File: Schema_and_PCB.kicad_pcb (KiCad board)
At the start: 2 copper layers, 0 parts

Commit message: board setup is done
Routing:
- net (no net): vias 0 -> 1
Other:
- copper layers 2 -> 4
- net class Default: trace_width 0.25 -> 0.2; via_dia 0.8 -> 0.6; via_drill 0.4 -> 0.3
- net class Power added: clearance 0.2, trace_width 0.6, via_dia 0.6, via_drill 0.3
- net class Thin added: clearance 0.2, trace_width 0.15, via_dia 0.6, via_drill 0.3
- rule trace_min: 0.15 -> 0.125
- rule via_min_size: 0.4 -> 0.3
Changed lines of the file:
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@@
 (kicad_pcb (version 20171130) (host pcbnew 5.1.10-88a1d61d58~88~ubuntu20.04.1)
   (general
-    (thickness 1.6)
+    (thickness 2)
     (drawings 0)
-    (tracks 0)
+    (tracks 1)
     (zones 0)
     (modules 0)
     (nets 1)
   )
-  (page A4)
+  (page A3)
   (title_block
-    (date 2021-03-19)
+    (title ШВУ)
+    (date 2021-05-21)
+    (rev v0.1)
+    (company SVIELCOM)
   )
   (layers
-    (0 F.Cu signal)
-    (31 B.Cu signal)
+    (0 F.Cu mixed)
+    (1 In1.Cu jumper)
+    (2 In2.Cu mixed)
+    (31 B.Cu mixed)
     (32 B.Adhes user)
     (33 F.Adhes user)
@@
   )
   (setup
-    (last_trace_width 0.25)
+    (last_trace_width 0.2)
     (user_trace_width 0.15)
+    (user_trace_width 0.2)
+    (user_trace_width 0.6)
     (trace_clearance 0.2)
     (zone_clearance 0.508)
     (zone_45_only no)
-    (trace_min 0.15)
-    (via_size 0.8)
-    (via_drill 0.4)
-    (via_min_size 0.4)
+    (trace_min 0.125)
+    (via_size 0.6)
+    (via_drill 0.3)
+    (via_min_size 0.3)
     (via_min_drill 0.3)
+    (user_via 0.6 0.3)
+    (user_via 0.8 0.5)
     (uvia_size 0.3)
     (uvia_drill 0.1)
@@
     (uvia_min_drill 0.1)
     (edge_width 0.1)
-    (segment_width 0.2)
+    (segment_width 0.25)
     (pcb_text_width 0.3)
     (pcb_text_size 1.5 1.5)
@@
   (net_class Default "This is the default net class."
     (clearance 0.2)
-    (trace_width 0.25)
-    (via_dia 0.8)
-    (via_drill 0.4)
+    (trace_width 0.2)
+    (via_dia 0.6)
+    (via_drill 0.3)
     (uvia_dia 0.3)
     (uvia_drill 0.1)
   )
+  (net_class Power ""
+    (clearance 0.2)
+    (trace_width 0.6)
+    (via_dia 0.6)
+    (via_drill 0.3)
+    (uvia_dia 0.3)
+    (uvia_drill 0.1)
+  )
+  (net_class Thin ""
+    (clearance 0.2)
+    (trace_width 0.15)
+    (via_dia 0.6)
+    (via_drill 0.3)
+    (uvia_dia 0.3)
+    (uvia_drill 0.1)
+  )
+  (via (at 169.4688 109.0676) (size 0.6) (drill 0.3) (layers F.Cu B.Cu) (net 0))
 )

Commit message: board shape is done
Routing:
- net (no net): vias 1 -> 0
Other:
- board outline added: 294.6 x 143.3 mm
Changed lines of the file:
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@@
   (general
     (thickness 2)
-    (drawings 0)
-    (tracks 1)
+    (drawings 41)
+    (tracks 0)
     (zones 0)
     (modules 0)
@@
     (uvia_drill 0.1)
   )
-  (via (at 169.4688 109.0676) (size 0.6) (drill 0.3) (layers F.Cu B.Cu) (net 0))
+  (gr_circle (center 347.726 92.9259) (end 349.7326 92.9259) (layer Edge.Cuts) (width 0.1))
+  (gr_circle (center 347.726 187.9346) (end 349.7326 187.9346) (layer Edge.Cuts) (width 0.1))
+  (gr_circle (center 215.6079 161.4551) (end 217.6145 161.4551) (layer Edge.Cuts) (width 0.1))
+  (gr_circle (center 68.6562 191.0969) (end 70.6628 191.0969) (layer Edge.Cuts) (width 0.1))
+  (gr_circle (center 68.6562 96.1009) (end 70.6628 96.1009) (layer Edge.Cuts) (width 0.1))
+  (gr_arc (start 63.0682 200.0123) (end 61.6458 200.0123) (angle -90) (layer Edge.Cuts) (width 0.1))
+  (gr_arc (start 81.2165 202.8571) (end 82.6389 202.8571) (angle -90) (layer Edge.Cuts) (width 0.1))
+  (gr_arc (start 84.0613 213.0171) (end 82.6389 213.0171) (angle -90) (layer Edge.Cuts) (width 0.1))
+  (gr_arc (start 193.8147 213.0171) (end 193.8147 214.4395) (angle -90) (layer Edge.Cuts) (width 0.1))
+  (gr_arc (start 196.6595 182.0926) (end 196.6595 180.6702) (angle -90) (layer Edge.Cuts) (width 0.1))
+  (gr_arc (start 337.82 182.0926) (end 339.2424 182.0926) (angle -90) (layer Edge.Cuts) (width 0.1))
+  (gr_arc (start 340.6648 194.9323) (end 339.2424 194.9323) (angle -90) (layer Edge.Cuts) (width 0.1))
+  (gr_arc (start 354.8126 194.9323) (end 354.8126 196.3547) (angle -90) (layer Edge.Cuts) (width 0.1))
+  (gr_arc (start 354.8126 86.8172) (end 356.235 86.8172) (angle -90) (layer Edge.Cuts) (width 0.1))
+  (gr_arc (start 333.6544 83.9724) (end 332.232 83.9724) (angle -90) (layer Edge.Cuts) (width 0.1))
+  (gr_arc (start 330.8096 72.5297) (end 332.232 72.5297) (angle -90) (layer Edge.Cuts) (width 0.1))
+  (gr_arc (start 220.6498 72.5297) (end 220.6498 71.1073) (angle -90) (layer Edge.Cuts) (width 0.1))
+  (gr_arc (start 217.805 78.6511) (end 217.805 80.0735) (angle -90) (layer Edge.Cuts) (width 0.1))
+  (gr_arc (start 192.7987 72.5297) (end 194.2211 72.5297) (angle -90) (layer Edge.Cuts) (width 0.1))
+  (gr_arc (start 195.6435 78.6511) (end 194.2211 78.6511) (angle -90) (layer Edge.Cuts) (width 0.1))
+  (gr_arc (start 84.074 72.5297) (end 84.074 71.1073) (angle -90) (layer Edge.Cuts) (width 0.1))
+  (gr_arc (start 63.0682 87.4649) (end 63.0682 86.0425) (angle -90) (layer Edge.Cuts) (width 0.1))
+  (gr_arc (start 81.2292 84.6201) (end 81.2292 86.0425) (angle -90) (layer Edge.Cuts) (width 0.1))
+  (gr_line (start 356.235 86.8172) (end 356.235 194.9323) (layer Edge.Cuts) (width 0.1))
+  (gr_line (start 333.6544 85.3948) (end 354.8126 85.3948) (layer Edge.Cuts) (width 0.1))
+  (gr_line (start 332.232 72.5297) (end 332.232 83.9724) (layer Edge.Cuts) (width 0.1))
+  (gr_line (start 220.6498 71.1073) (end 330.8096 71.1073) (layer Edge.Cuts) (width 0.1))
+  (gr_line (start 219.2274 78.6511) (end 219.2274 72.5297) (layer Edge.Cuts) (width 0.1))
+  (gr_line (start 195.6435 80.0735) (end 217.805 80.0735) (layer Edge.Cuts) (width 0.1))
+  (gr_line (start 194.2211 72.5297) (end 194.2211 78.6511) (layer Edge.Cuts) (width 0.1))
+  (gr_line (start 84.074 71.1073) (end 192.7987 71.1073) (layer Edge.Cuts) (width 0.1))
+  (gr_line (start 82.6516 84.6201) (end 82.6516 72.5297) (layer Edge.Cuts) (width 0.1))
+  (gr_line (start 63.0682 86.0425) (end 81.2292 86.0425) (layer Edge.Cuts) (width 0.1))
+  (gr_line (start 61.6458 200.0123) (end 61.6458 87.4649) (layer Edge.Cuts) (width 0.1))
+  (gr_line (start 81.2165 201.4347) (end 63.0682 201.4347) (layer Edge.Cuts) (width 0.1))
+  (gr_line (start 82.6389 213.0171) (end 82.6389 202.8571) (layer Edge.Cuts) (width 0.1))
+  (gr_line (start 193.8147 214.4395) (end 84.0613 214.4395) (layer Edge.Cuts) (width 0.1))
+  (gr_line (start 195.2371 182.0926) (end 195.2371 213.0171) (layer Edge.Cuts) (width 0.1))
+  (gr_line (start 337.82 180.6702) (end 196.6595 180.6702) (layer Edge.Cuts) (width 0.1))
+  (gr_line (start 339.2424 194.9323) (end 339.2424 182.0926) (layer Edge.Cuts) (width 0.1))
+  (gr_line (start 354.8126 196.3547) (end 340.6648 196.3547) (layer Edge.Cuts) (width 0.1))
 )

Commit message: starting PCB layout
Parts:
- added BT1: CR2032, SVIELCOM:BAT_BS-7, F.Cu at (13.6, 21.3)
- added C1: 10µF, Capacitor_Tantalum_SMD:CP_EIA-3216-10_Kemet-I, F.Cu at (250.7, 253.4)
- added C10: 2,7pF, Capacitor_SMD:C_0603_1608Metric_Pad1.08x0.95mm_HandSolder, F.Cu at (24.8, 40.1)
- added C11: 47µFx16, Capacitor_Tantalum_SMD:CP_EIA-7343-31_Kemet-D_Pad2.25x2.55mm_HandSolder, F.Cu at (16.2, 45.8)
- added C12: 10µFx16, Capacitor_Tantalum_SMD:CP_EIA-3216-10_Kemet-I, F.Cu at (34.5, 47.6)
- added C13: 1µF, Capacitor_SMD:C_0603_1608Metric_Pad1.08x0.95mm_HandSolder, F.Cu at (66.5, 23.7)
- added C14: 0,1µF, Capacitor_SMD:C_0603_1608Metric_Pad1.08x0.95mm_HandSolder, F.Cu at (68.6, 26.2)
- added C15: 47µFx16, Capacitor_Tantalum_SMD:CP_EIA-7343-31_Kemet-D_Pad2.25x2.55mm_HandSolder, F.Cu at (26.5, 45.8)
- added C16: 10µFx16, Capacitor_Tantalum_SMD:CP_EIA-3216-10_Kemet-I, F.Cu at (43.4, 43.0)
- added C17: 1µF, Capacitor_SMD:C_0603_1608Metric_Pad1.08x0.95mm_HandSolder, F.Cu at (61.4, 37.8)
- added C18: 1µF, Capacitor_SMD:C_0603_1608Metric_Pad1.08x0.95mm_HandSolder, F.Cu at (57.1, 40.3)
- added C19: 1µF, Capacitor_SMD:C_0603_1608Metric_Pad1.08x0.95mm_HandSolder, F.Cu at (68.6, 28.7)
- added C2: 1µF, Capacitor_SMD:C_0603_1608Metric_Pad1.08x0.95mm_HandSolder, F.Cu at (246.0, 253.2)
- added C20: 1µF, Capacitor_SMD:C_0603_1608Metric_Pad1.08x0.95mm_HandSolder, F.Cu at (61.6, 35.3)
- added C21: 1µF, Capacitor_SMD:C_0603_1608Metric_Pad1.08x0.95mm_HandSolder, F.Cu at (71.3, 20.8)
- added C22: 1µF, Capacitor_SMD:C_0603_1608Metric_Pad1.08x0.95mm_HandSolder, F.Cu at (48.2, 47.7)
- added C23: 1µF, Capacitor_SMD:C_0603_1608Metric_Pad1.08x0.95mm_HandSolder, F.Cu at (61.6, 32.8)
- added C24: 1µF, Capacitor_SMD:C_0603_1608Metric_Pad1.08x0.95mm_HandSolder, F.Cu at (43.8, 48.4)
- added C25: 1µF, Capacitor_SMD:C_0603_1608Metric_Pad1.08x0.95mm_HandSolder, F.Cu at (42.7, 50.9)
- added C26: 1µF, Capacitor_SMD:C_0603_1608Metric_Pad1.08x0.95mm_HandSolder, F.Cu at (70.9, 23.3)
- added C27: 1µF, Capacitor_SMD:C_0603_1608Metric_Pad1.08x0.95mm_HandSolder, F.Cu at (57.1, 37.8)
- added C28: 10µF, Capacitor_Tantalum_SMD:CP_EIA-3216-10_Kemet-I, F.Cu at (34.5, 44.5)
- added C29: 2,2µF, Capacitor_SMD:C_0603_1608Metric_Pad1.08x0.95mm_HandSolder, F.Cu at (57.3, 35.3)
- added C3: 1µF, Capacitor_SMD:C_0603_1608Metric_Pad1.08x0.95mm_HandSolder, F.Cu at (291.1, 248.5)
- added C30: 2,2µF, Capacitor_SMD:C_0603_1608Metric_Pad1.08x0.95mm_HandSolder, F.Cu at (64.3, 28.7)
- added C31: 1µF, Capacitor_SMD:C_0603_1608Metric_Pad1.08x0.95mm_HandSolder, F.Cu at (48.4, 45.2)
- added C32: 10µF, Capacitor_Tantalum_SMD:CP_EIA-3216-10_Kemet-I, F.Cu at (23.0, 50.3)
- added C33: 1µF, Capacitor_SMD:C_0603_1608Metric_Pad1.08x0.95mm_HandSolder, F.Cu at (52.7, 43.5)
- added C34: 10µF, Capacitor_Tantalum_SMD:CP_EIA-3216-10_Kemet-I, F.Cu at (61.6, 19.4)
- added C35: 1µF, Capacitor_SMD:C_0603_1608Metric_Pad1.08x0.95mm_HandSolder, F.Cu at (64.3, 26.2)
- added C36: 1µF, Capacitor_SMD:C_0603_1608Metric_Pad1.08x0.95mm_HandSolder, F.Cu at (57.3, 32.8)
- added C37: 1µF, Capacitor_SMD:C_0603_1608Metric_Pad1.08x0.95mm_HandSolder, F.Cu at (52.5, 37.4)
- added C38: 1µF, Capacitor_SMD:C_0603_1608Metric_Pad1.08x0.95mm_HandSolder, F.Cu at (59.5, 30.3)
- added C39: 1µF, Capacitor_SMD:C_0603_1608Metric_Pad1.08x0.95mm_HandSolder, F.Cu at (71.3, 18.2)
- added C4: 1µF, Capacitor_SMD:C_0603_1608Metric_Pad1.08x0.95mm_HandSolder, F.Cu at (306.1, 240.5)
- added C40: 1µF, Capacitor_SMD:C_0603_1608Metric_Pad1.08x0.95mm_HandSolder, F.Cu at (43.8, 45.9)
- added C41: 1µF, Capacitor_SMD:C_0603_1608Metric_Pad1.08x0.95mm_HandSolder, F.Cu at (38.4, 50.9)
- added C42: 1µF, Capacitor_SMD:C_0603_1608Metric_Pad1.08x0.95mm_HandSolder, F.Cu at (39.5, 48.4)
- added C43: 1µF, Capacitor_SMD:C_0603_1608Metric_Pad1.08x0.95mm_HandSolder, F.Cu at (39.5, 45.9)
- added C44: 1µF, Capacitor_SMD:C_0603_1608Metric_Pad1.08x0.95mm_HandSolder, F.Cu at (24.8, 37.6)
- added C45: 1µF, Capacitor_SMD:C_0603_1608Metric_Pad1.08x0.95mm_HandSolder, F.Cu at (97.9, 57.7)
- added C46: 1µF, Capacitor_SMD:C_0603_1608Metric_Pad1.08x0.95mm_HandSolder, F.Cu at (211.2, 252.7)
- added C47: 1µF, Capacitor_SMD:C_0603_1608Metric_Pad1.08x0.95mm_HandSolder, F.Cu at (220.0, 252.9)
- added C48: 1µF, Capacitor_SMD:C_0603_1608Metric_Pad1.08x0.95mm_HandSolder, F.Cu at (16.2, -10.9)
- added C49: 10µFx35, Capacitor_Tantalum_SMD:CP_EIA-7343-30_AVX-N_Pad2.25x2.55mm_HandSolder, F.Cu at (31.4, -2.06)
- added C5: 4,6pF, Capacitor_SMD:C_0603_1608Metric_Pad1.08x0.95mm_HandSolder, F.Cu at (24.8, 35.0)
- added C50: 1µF, Capacitor_SMD:C_0603_1608Metric_Pad1.08x0.95mm_HandSolder, F.Cu at (38.2, -13.5)
- added C51: 10µFx35, Capacitor_Tantalum_SMD:CP_EIA-7343-30_AVX-N_Pad2.25x2.55mm_HandSolder, F.Cu at (16.5, 1.91)
- added C52: 1µF, Capacitor_SMD:C_0603_1608Metric_Pad1.08x0.95mm_HandSolder, F.Cu at (33.9, -13.5)
- added C53: 10µFx16, Capacitor_Tantalum_SMD:CP_EIA-3216-10_Kemet-I, F.Cu at (52.4, -35.6)
- added C54: 0,1µF, Capacitor_SMD:C_0603_1608Metric_Pad1.08x0.95mm_HandSolder, F.Cu at (29.5, -13.5)
- added C55: 0,1µF, Capacitor_SMD:C_0603_1608Metric_Pad1.08x0.95mm_HandSolder, F.Cu at (9.17, 4.04)
- added C56: 0,22µF, Capacitor_SMD:C_0603_1608Metric_Pad1.08x0.95mm_HandSolder, F.Cu at (59.5, 1.89)
- added C57: 330pF, Capacitor_SMD:C_0603_1608Metric_Pad1.08x0.95mm_HandSolder, F.Cu at (72.3, -9.30)
- added C58: 1µF, Capacitor_SMD:C_0603_1608Metric_Pad1.08x0.95mm_HandSolder, F.Cu at (89.9, -28.4)
- added C59: 1µF, Capacitor_SMD:C_0603_1608Metric_Pad1.08x0.95mm_HandSolder, F.Cu at (80.9, -18.1)
- added C6: 4,6pF, Capacitor_SMD:C_0603_1608Metric_Pad1.08x0.95mm_HandSolder, F.Cu at (48.4, 42.7)
- added C60: 10µFx35, Capacitor_Tantalum_SMD:CP_EIA-7343-30_AVX-N_Pad2.25x2.55mm_HandSolder, F.Cu at (69.6, -50.5)
- added C61: 1µF, Capacitor_SMD:C_0603_1608Metric_Pad1.08x0.95mm_HandSolder, F.Cu at (98.3, -36.6)
- added C62: 1µF, Capacitor_SMD:C_0603_1608Metric_Pad1.08x0.95mm_HandSolder, F.Cu at (76.2, -14.7)
- added C63: 0,1µF, Capacitor_SMD:C_0603_1608Metric_Pad1.08x0.95mm_HandSolder, F.Cu at (96.8, -33.9)
- added C64: 0,22µF, Capacitor_SMD:C_0603_1608Metric_Pad1.08x0.95mm_HandSolder, F.Cu at (85.7, -24.0)
- added C65: 330pF, Capacitor_SMD:C_0603_1608Metric_Pad1.08x0.95mm_HandSolder, F.Cu at (59.4, -3.13)
- added C66: 0,1µF, Capacitor_SMD:C_0603_1608Metric_Pad1.08x0.95mm_HandSolder, F.Cu at (63.8, -0.62)
- added C67: 1µF, Capacitor_SMD:C_0603_1608Metric_Pad1.08x0.95mm_HandSolder, F.Cu at (89.9, -30.9)
- added C68: 1µF, Capacitor_SMD:C_0603_1608Metric_Pad1.08x0.95mm_HandSolder, F.Cu at (59.5, -0.62)
- added C69: 1µF, Capacitor_SMD:C_0603_1608Metric_Pad1.08x0.95mm_HandSolder, F.Cu at (67.5, -6.35)
- added C7: 2,7pF, Capacitor_SMD:C_0603_1608Metric_Pad1.08x0.95mm_HandSolder, F.Cu at (66.5, 21.2)
- added C70: 1µF, Capacitor_SMD:C_0603_1608Metric_Pad1.08x0.95mm_HandSolder, F.Cu at (98.3, -41.6)
- added C71: 1µF, Capacitor_SMD:C_0603_1608Metric_Pad1.08x0.95mm_HandSolder, F.Cu at (85.2, -26.5)
- added C72: 10µFx35, Capacitor_Tantalum_SMD:CP_EIA-7343-30_AVX-N_Pad2.25x2.55mm_HandSolder, F.Cu at (79.8, -50.5)
- added C73: 1µF, Capacitor_SMD:C_0603_1608Metric_Pad1.08x0.95mm_HandSolder, F.Cu at (20.6, -10.9)
- added C74: 0,1µF, Capacitor_SMD:C_0603_1608Metric_Pad1.08x0.95mm_HandSolder, F.Cu at (92.5, -33.9)
- added C75: 1µF, Capacitor_SMD:C_0603_1608Metric_Pad1.08x0.95mm_HandSolder, F.Cu at (76.2, -17.2)
- added C76: 0,1µF, Capacitor_SMD:C_0603_1608Metric_Pad1.08x0.95mm_HandSolder, F.Cu at (98.3, -39.1)
- added C77: 0,22µF, Capacitor_SMD:C_0603_1608Metric_Pad1.08x0.95mm_HandSolder, F.Cu at (63.8, -3.13)
- added C78: 330pF, Capacitor_SMD:C_0603_1608Metric_Pad1.08x0.95mm_HandSolder, F.Cu at (80.9, -20.6)
- added C79: 0,1µF, Capacitor_SMD:C_0603_1608Metric_Pad1.08x0.95mm_HandSolder, F.Cu at (275.5, 231.6)
- added C8: 10µFx16, Capacitor_Tantalum_SMD:CP_EIA-3216-10_Kemet-I, F.Cu at (17.3, 50.3)
- added C80: 0,1µF, Capacitor_SMD:C_0603_1608Metric_Pad1.08x0.95mm_HandSolder, F.Cu at (287.2, 226.4)
- added C81: 0,1µF, Capacitor_SMD:C_0603_1608Metric_Pad1.08x0.95mm_HandSolder, F.Cu at (271.1, 231.6)
- added C82: 0,1µF, Capacitor_SMD:C_0603_1608Metric_Pad1.08x0.95mm_HandSolder, F.Cu at (295.2, 215.3)
- added C83: 0,1µF, Capacitor_SMD:C_0603_1608Metric_Pad1.08x0.95mm_HandSolder, F.Cu at (285.4, 231.4)
- added C84: 0,1µF, Capacitor_SMD:C_0603_1608Metric_Pad1.08x0.95mm_HandSolder, F.Cu at (285.4, 228.9)
- added C85: 1µF, Capacitor_SMD:C_0603_1608Metric_Pad1.08x0.95mm_HandSolder, F.Cu at (251.5, 233.0)
- added C86: 1µF, Capacitor_SMD:C_0603_1608Metric_Pad1.08x0.95mm_HandSolder, F.Cu at (264.3, 215.3)
- added C87: 1µF, Capacitor_SMD:C_0603_1608Metric_Pad1.08x0.95mm_HandSolder, F.Cu at (261.9, 225.2)
- added C88: 10µF, Capacitor_Tantalum_SMD:CP_EIA-3216-10_Kemet-I, F.Cu at (220.7, 244.9)
- added C89: 1µF, Capacitor_SMD:C_0603_1608Metric_Pad1.08x0.95mm_HandSolder, F.Cu at (256.1, 231.3)
- added C9: 10µFx16, Capacitor_Tantalum_SMD:CP_EIA-3216-10_Kemet-I, F.Cu at (28.6, 50.3)
- added C90: 1µF, Capacitor_SMD:C_0603_1608Metric_Pad1.08x0.95mm_HandSolder, F.Cu at (260.8, 228.4)
- added C91: 1µF, Capacitor_SMD:C_0603_1608Metric_Pad1.08x0.95mm_HandSolder, F.Cu at (250.2, 238.9)
- added C92: 5,6pF, Capacitor_SMD:C_0603_1608Metric_Pad1.08x0.95mm_HandSolder, F.Cu at (233.9, 250.5)
- added C93: 1µF, Capacitor_SMD:C_0603_1608Metric_Pad1.08x0.95mm_HandSolder, F.Cu at (251.5, 235.6)
- added C94: 470pF, Capacitor_SMD:C_0603_1608Metric_Pad1.08x0.95mm_HandSolder, F.Cu at (245.8, 238.9)
- added C95: 5,6pF, Capacitor_SMD:C_0603_1608Metric_Pad1.08x0.95mm_HandSolder, F.Cu at (229.5, 250.5)
- added D1: L-1154ID, LED_THT:LED_D3.0mm, F.Cu at (226.1, 201.1)
- added D10: 1N4743A, Diode_THT:D_DO-41_SOD81_P10.16mm_Horizontal, F.Cu at (14.6, -22.6)
- added D11: BZV85-C56.113, Diode_THT:D_DO-41_SOD81_P10.16mm_Horizontal, F.Cu at (14.6, -37.1)
- added D12: BZV85-C56.113, Diode_THT:D_DO-41_SOD81_P10.16mm_Horizontal, F.Cu at (37.5, -39.2)
- added D13: 1N4743A, Diode_THT:D_DO-41_SOD81_P10.16mm_Horizontal, F.Cu at (-0.63, 0.66)
- added D14: 1N4743A, Diode_THT:D_DO-41_SOD81_P10.16mm_Horizontal, F.Cu at (14.9, -7.19)
- added D15: USBLC6-4SC6, Package_TO_SOT_SMD:SOT-23-6_Handsoldering, F.Cu at (247.3, 226.5)
- added D2: L-1154ID, LED_THT:LED_D3.0mm, F.Cu at (220.2, 201.1)
- added D3: ESDA6V1BC6, Package_TO_SOT_SMD:SOT-23-6, F.Cu at (296.7, 238.6)
- added D4: 2W10G-E4/51, Diode_THT:Diode_Bridge_Round_D9.8mm, F.Cu at (44.0, -18.4)
- added D5: BZV85-C56.113, Diode_THT:D_DO-41_SOD81_P10.16mm_Horizontal, F.Cu at (30.1, -30.4)
- added D6: 1N4743A, Diode_THT:D_DO-41_SOD81_P10.16mm_Horizontal, F.Cu at (37.5, -43.4)
- added D7: 1N4743A, Diode_THT:D_DO-41_SOD81_P10.16mm_Horizontal, F.Cu at (37.5, -34.9)
- added D8: ES1G, Diode_SMD:D_SMA_Handsoldering, F.Cu at (79.9, -45.3)
- added D9: 1N4743A, Diode_THT:D_DO-41_SOD81_P10.16mm_Horizontal, F.Cu at (15.9, -18.3)
- added J1: USB4085-GF-A_REVA, SVIELCOM:GCT_USB4085-GF-A_REVA, F.Cu at (65.3, 177.6)
- added J10: 22-23-2021, digikey-footprints:PinHeader_1x2_P2.54mm_Drill1.02mm, F.Cu at (54.2, -15.9)
- added J11: Pulse_JXD6-0001NL, Connector_RJ:RJ45_Pulse_JXD6-0001NL_Horizontal, F.Cu at (71.8, 160.9)
- added J12: OSTTC020162, digikey-footprints:Term_Block_1x2_P5mm, F.Cu at (249.1, 212.7)
- added J13: 640456-2, digikey-footprints:PinHeader_1x2_P2.54mm_Drill1.02mm, F.Cu at (67.2, 139.2)
- added J14: 640456-3, digikey-footprints:PinHeader_1x3_P2.54_Drill1.1mm, F.Cu at (305.4, 188.8)
- added J15: 640456-3, digikey-footprints:PinHeader_1x3_P2.54_Drill1.1mm, F.Cu at (304.3, 194.9)
- added J16: 0022232041, digikey-footprints:PinHeader_1x4_P2.54mm_Drill1.02mm, F.Cu at (139.7, 74.4)
- added J17: 0022232041, digikey-footprints:PinHeader_1x4_P2.54mm_Drill1.02mm, F.Cu at (67.2, 128.5)
- added J2: OSTTC020162, digikey-footprints:Term_Block_1x2_P5mm, F.Cu at (55.8, 13.3)
- added J3: OSTTC020162, digikey-footprints:Term_Block_1x2_P5mm, F.Cu at (14.4, 38.3)
- added J4: DM3AT-SF-PEJM5, SVIELCOM:HRS_DM3AT-SF-PEJM5, F.Cu at (137.7, 197.0)
- added J5: OSTTC020162, digikey-footprints:Term_Block_1x2_P5mm, F.Cu at (58.8, -32.7)
- added J6: 22-23-2021, digikey-footprints:PinHeader_1x2_P2.54mm_Drill1.02mm, F.Cu at (38.5, 0.17)
- added J7: OSTTC030162, digikey-footprints:Term_Block_1x3_P5mm, F.Cu at (0.77, -13.8)
- added J8: 22-23-2021, digikey-footprints:PinHeader_1x2_P2.54mm_Drill1.02mm, F.Cu at (69.0, -26.3)
- added J9: 0022232031, digikey-footprints:PinHeader_1x3_P2.54mm_Drill1.02mm, F.Cu at (69.0, -34.2)
- added JP1: Jumper_3_Bridged12, Jumper:SolderJumper-3_P1.3mm_Open_RoundedPad1.0x1.5mm_NumberLabels, F.Cu at (61.5, 22.7)
- added JP2: JUMPER2, Jumper:SolderJumper-2_P1.3mm_Open_TrianglePad1.0x1.5mm, F.Cu at (52.7, 46.5)
- added JP3: Jumper_3_Bridged12, Connector_PinHeader_2.54mm:PinHeader_1x03_P2.54mm_Horizontal, F.Cu at (29.4, 35.5)
- added JP4: Jumper_3_Bridged12, Jumper:SolderJumper-3_P1.3mm_Open_RoundedPad1.0x1.5mm_NumberLabels, F.Cu at (55.3, 24.3)
- added JP5: Closed, Jumper:SolderJumper-2_P1.3mm_Open_RoundedPad1.0x1.5mm, F.Cu at (52.7, 40.4)
- added L1: 600R@100MHz [BK2125HS601-T], Inductor_SMD:L_0805_2012Metric_Pad1.15x1.40mm_HandSolder, F.Cu at (281.8, 236.6)
- added L2: 600R@100MHz [BK2125HS601-T], Inductor_SMD:L_0805_2012Metric_Pad1.15x1.40mm_HandSolder, F.Cu at (59.7, 27.6)
- added L3: B82790C0225N265, Inductor_SMD:L_CommonMode_Delevan_4222, F.Cu at (32.9, -8.56)
- added L4: B82790C0225N265, Inductor_SMD:L_CommonMode_Delevan_4222, F.Cu at (48.2, -25.2)
- added L5: B82790C0225N265, Inductor_SMD:L_CommonMode_Delevan_4222, F.Cu at (68.8, -41.7)
- added L6: 600R@100MHz [BK2125HS601-T], Inductor_SMD:L_0805_2012Metric_Pad1.15x1.40mm_HandSolder, F.Cu at (256.3, 228.6)
- added LS1: HCM1203X, Buzzer_Beeper:Buzzer_12x9.5RM7.6, F.Cu at (31.2, -21.5)
- added PS1: TMH2415S, Converter_DCDC:Converter_DCDC_XP_POWER-IAxxxxS_THT, F.Cu at (165.6, -13.9)
- added PS2: TMH2415S, Converter_DCDC:Converter_DCDC_XP_POWER-IAxxxxS_THT, F.Cu at (165.6, -61.3)
- added PS3: TMH2415S, Converter_DCDC:Converter_DCDC_XP_POWER-IAxxxxS_THT, F.Cu at (165.4, -37.7)
- added Q1: BC817-25LT1G, digikey-footprints:SOT-23-3, F.Cu at (237.4, 200.8)
- added Q2: BC817-25LT1G, digikey-footprints:SOT-23-3, F.Cu at (232.7, 200.8)
- added Q3: BC817-25LT1G, digikey-footprints:SOT-23-3, F.Cu at (45.4, -1.30)
- added Q4: BC817-25LT1G, digikey-footprints:SOT-23-3, F.Cu at (61.1, -12.8)
- added R1: 100, Resistor_SMD:R_0805_2012Metric_Pad1.20x1.40mm_HandSolder, F.Cu at (265.9, 199.8)
- added R10: 24, Resistor_SMD:R_0805_2012Metric_Pad1.20x1.40mm_HandSolder, F.Cu at (257.3, 251.0)
- added R100: 10K, Resistor_SMD:R_0805_2012Metric_Pad1.20x1.40mm_HandSolder, F.Cu at (220.2, 248.0)
- added R101: 33, Resistor_SMD:R_0805_2012Metric_Pad1.20x1.40mm_HandSolder, F.Cu at (252.6, 225.7)
- added R102: 33, Resistor_SMD:R_0805_2012Metric_Pad1.20x1.40mm_HandSolder, F.Cu at (241.7, 244.9)
- added R103: 12,1K, Resistor_SMD:R_0805_2012Metric_Pad1.20x1.40mm_HandSolder, F.Cu at (259.7, 212.6)
- added R11: 24, Resistor_SMD:R_0805_2012Metric_Pad1.20x1.40mm_HandSolder, F.Cu at (279.3, 248.3)
- added R12: 24, Resistor_SMD:R_0805_2012Metric_Pad1.20x1.40mm_HandSolder, F.Cu at (301.5, 237.8)
- added R13: 24, Resistor_SMD:R_0805_2012Metric_Pad1.20x1.40mm_HandSolder, F.Cu at (272.4, 248.7)
- added R14: 5,1K, Resistor_SMD:R_0805_2012Metric_Pad1.20x1.40mm_HandSolder, F.Cu at (262.6, 237.1)
- added R15: 5,1K, Resistor_SMD:R_0805_2012Metric_Pad1.20x1.40mm_HandSolder, F.Cu at (267.0, 250.0)
- added R16: 10K, Resistor_SMD:R_0805_2012Metric_Pad1.20x1.40mm_HandSolder, F.Cu at (66.7, 18.5)
- added R17: 10K, Resistor_SMD:R_0805_2012Metric_Pad1.20x1.40mm_HandSolder, F.Cu at (52.7, 34.7)
- added R18: 47, Resistor_SMD:R_0805_2012Metric_Pad1.20x1.40mm_HandSolder, F.Cu at (33.8, 50.7)
- added R19: 33, Resistor_SMD:R_0805_2012Metric_Pad1.20x1.40mm_HandSolder, F.Cu at (98.1, 55.0)
- added R2: 100, Resistor_SMD:R_0805_2012Metric_Pad1.20x1.40mm_HandSolder, F.Cu at (242.1, 202.7)
- added R20: 33, Resistor_SMD:R_0805_2012Metric_Pad1.20x1.40mm_HandSolder, F.Cu at (102.8, 52.1)
- added R21: 33, Resistor_SMD:R_0805_2012Metric_Pad1.20x1.40mm_HandSolder, F.Cu at (215.1, 256.8)
- added R22: 33, Resistor_SMD:R_0805_2012Metric_Pad1.20x1.40mm_HandSolder, F.Cu at (98.1, 52.1)
- added R23: 82K, Resistor_THT:R_Axial_DIN0207_L6.3mm_D2.5mm_P10.16mm_Horizontal, F.Cu at (51.1, -39.2)
- added R24: 3,3K, Resistor_SMD:R_0805_2012Metric_Pad1.20x1.40mm_HandSolder, F.Cu at (54.9, 3.60)
- added R25: 825, Resistor_SMD:R_0805_2012Metric_Pad1.20x1.40mm_HandSolder, F.Cu at (81.1, -23.4)
- added R26: 560, Resistor_SMD:R_0805_2012Metric_Pad1.20x1.40mm_HandSolder, F.Cu at (76.4, -19.9)
- added R27: 15K, Resistor_THT:R_Axial_DIN0207_L6.3mm_D2.5mm_P10.16mm_Horizontal, F.Cu at (15.6, -14.2)
- added R28: 1K, Resistor_THT:R_Axial_DIN0207_L6.3mm_D2.5mm_P10.16mm_Horizontal, F.Cu at (52.7, -51.4)
- added R29: 10K, Resistor_SMD:R_0805_2012Metric_Pad1.20x1.40mm_HandSolder, F.Cu at (93.6, -42.5)
- added R3: 200, Resistor_SMD:R_0805_2012Metric_Pad1.20x1.40mm_HandSolder, F.Cu at (270.6, 199.8)
- added R30: 1,1K, Resistor_SMD:R_0805_2012Metric_Pad1.20x1.40mm_HandSolder, F.Cu at (76.4, -22.9)
- added R31: 10K, Resistor_SMD:R_0805_2012Metric_Pad1.20x1.40mm_HandSolder, F.Cu at (85.4, -29.3)
- added R32: 825, Resistor_SMD:R_0805_2012Metric_Pad1.20x1.40mm_HandSolder, F.Cu at (98.4, -44.3)
- added R33: 10K, Resistor_SMD:R_0805_2012Metric_Pad1.20x1.40mm_HandSolder, F.Cu at (87.9, -33.7)
- added R34: 10K, Resistor_SMD:R_0805_2012Metric_Pad1.20x1.40mm_HandSolder, F.Cu at (54.9, 0.65)
- added R35: 3,3K, Resistor_SMD:R_0805_2012Metric_Pad1.20x1.40mm_HandSolder, F.Cu at (71.6, -15.0)
- added R36: 2K, Resistor_SMD:R_0805_2012Metric_Pad1.20x1.40mm_HandSolder, F.Cu at (80.6, -26.3)
- added R37: 1K, Resistor_SMD:R_0805_2012Metric_Pad1.20x1.40mm_HandSolder, F.Cu at (93.7, -39.6)
- added R38: 1K, Resistor_SMD:R_0805_2012Metric_Pad1.20x1.40mm_HandSolder, F.Cu at (65.8, -12.0)
- added R39: 1K, Resistor_SMD:R_0805_2012Metric_Pad1.20x1.40mm_HandSolder, F.Cu at (54.9, -2.30)
- added R4: 47K, Resistor_SMD:R_0805_2012Metric_Pad1.20x1.40mm_HandSolder, F.Cu at (242.1, 199.8)
- added R40: 10K, Resistor_SMD:R_0805_2012Metric_Pad1.20x1.40mm_HandSolder, F.Cu at (96.8, -47.3)
- added R41: 3,3K, Resistor_SMD:R_0805_2012Metric_Pad1.20x1.40mm_HandSolder, F.Cu at (58.2, -8.81)
- added R42: 825, Resistor_SMD:R_0805_2012Metric_Pad1.20x1.40mm_HandSolder, F.Cu at (71.6, -20.9)
- added R43: 10K, Resistor_SMD:R_0805_2012Metric_Pad1.20x1.40mm_HandSolder, F.Cu at (80.6, -29.3)
- added R44: 1K, Resistor_THT:R_Axial_DIN0207_L6.3mm_D2.5mm_P10.16mm_Horizontal, F.Cu at (51.1, -43.3)
- added R45: 10K, Resistor_SMD:R_0805_2012Metric_Pad1.20x1.40mm_HandSolder, F.Cu at (67.7, -9.08)
- added R46: 1,1K, Resistor_SMD:R_0805_2012Metric_Pad1.20x1.40mm_HandSolder, F.Cu at (83.2, -32.2)
- added R47: 10K, Resistor_SMD:R_0805_2012Metric_Pad1.20x1.40mm_HandSolder, F.Cu at (89.0, -39.6)
- added R48: 825, Resistor_SMD:R_0805_2012Metric_Pad1.20x1.40mm_HandSolder, F.Cu at (87.3, -45.5)
- added R49: 10K, Resistor_SMD:R_0805_2012Metric_Pad1.20x1.40mm_HandSolder, F.Cu at (75.9, -25.8)
- added R5: 47K, Resistor_SMD:R_0805_2012Metric_Pad1.20x1.40mm_HandSolder, F.Cu at (251.6, 199.8)
- added R50: 10K, Resistor_SMD:R_0805_2012Metric_Pad1.20x1.40mm_HandSolder, F.Cu at (66.9, -17.9)
- added R51: 3,3K, Resistor_SMD:R_0805_2012Metric_Pad1.20x1.40mm_HandSolder, F.Cu at (66.9, -20.9)
- added R52: 2K, Resistor_SMD:R_0805_2012Metric_Pad1.20x1.40mm_HandSolder, F.Cu at (45.4, 2.65)
- added R53: 1K, Resistor_SMD:R_0805_2012Metric_Pad1.20x1.40mm_HandSolder, F.Cu at (50.1, -2.30)
- added R54: 1K, Resistor_SMD:R_0805_2012Metric_Pad1.20x1.40mm_HandSolder, F.Cu at (66.9, -15.0)
- added R55: 1K, Resistor_SMD:R_0805_2012Metric_Pad1.20x1.40mm_HandSolder, F.Cu at (75.9, -28.8)
- added R56: 560, Resistor_SMD:R_0805_2012Metric_Pad1.20x1.40mm_HandSolder, F.Cu at (78.4, -32.2)
- added R57: 10K, Resistor_THT:R_Axial_DIN0207_L6.3mm_D2.5mm_P10.16mm_Horizontal, F.Cu at (52.7, -47.3)
- added R58: 3,3K, Resistor_SMD:R_0805_2012Metric_Pad1.20x1.40mm_HandSolder, F.Cu at (84.2, -36.9)
- added R59: 825, Resistor_SMD:R_0805_2012Metric_Pad1.20x1.40mm_HandSolder, F.Cu at (88.9, -42.5)
- added R6: 16,9K, Resistor_SMD:R_0805_2012Metric_Pad1.20x1.40mm_HandSolder, F.Cu at (256.4, 199.8)
- added R60: 560, Resistor_SMD:R_0805_2012Metric_Pad1.20x1.40mm_HandSolder, F.Cu at (92.0, -45.5)
- added R61: 10K, Resistor_THT:R_Axial_DIN0207_L6.3mm_D2.5mm_P10.16mm_Horizontal, F.Cu at (43.8, -30.8)
- added R62: 1K, Resistor_THT:R_Axial_DIN0207_L6.3mm_D2.5mm_P10.16mm_Horizontal, F.Cu at (14.6, -3.04)
- added R63: 10K, Resistor_SMD:R_0805_2012Metric_Pad1.20x1.40mm_HandSolder, F.Cu at (4.62, 4.26)
- added R64: 1,1K, Resistor_SMD:R_0805_2012Metric_Pad1.20x1.40mm_HandSolder, F.Cu at (-0.13, 4.26)
- added R65: 10K, Resistor_SMD:R_0805_2012Metric_Pad1.20x1.40mm_HandSolder, F.Cu at (70.5, -12.0)
- added R66: 825, Resistor_SMD:R_0805_2012Metric_Pad1.20x1.40mm_HandSolder, F.Cu at (63.0, -5.86)
- added R67: 10K, Resistor_SMD:R_0805_2012Metric_Pad1.20x1.40mm_HandSolder, F.Cu at (93.7, -36.6)
- added R68: 10K, Resistor_SMD:R_0805_2012Metric_Pad1.20x1.40mm_HandSolder, F.Cu at (58.2, -5.86)
- added R69: 3,3K, Resistor_SMD:R_0805_2012Metric_Pad1.20x1.40mm_HandSolder, F.Cu at (63.0, -8.81)
- added R7: 200, Resistor_SMD:R_0805_2012Metric_Pad1.20x1.40mm_HandSolder, F.Cu at (261.1, 199.8)
- added R70: 2K, Resistor_SMD:R_0805_2012Metric_Pad1.20x1.40mm_HandSolder, F.Cu at (89.0, -36.6)
- added R71: 1K, Resistor_SMD:R_0805_2012Metric_Pad1.20x1.40mm_HandSolder, F.Cu at (71.6, -17.9)
- added R72: 1K, Resistor_SMD:R_0805_2012Metric_Pad1.20x1.40mm_HandSolder, F.Cu at (50.2, 0.65)
- added R73: 1K, Resistor_SMD:R_0805_2012Metric_Pad1.20x1.40mm_HandSolder, F.Cu at (50.2, 3.60)
- added R74: 15K, Resistor_SMD:R_0805_2012Metric_Pad1.20x1.40mm_HandSolder, F.Cu at (280.8, 230.7)
- added R75: 15K, Resistor_SMD:R_0805_2012Metric_Pad1.20x1.40mm_HandSolder, F.Cu at (276.1, 228.9)
- added R76: 15K, Resistor_SMD:R_0805_2012Metric_Pad1.20x1.40mm_HandSolder, F.Cu at (271.3, 228.9)
- added R77: 15K, Resistor_SMD:R_0805_2012Metric_Pad1.20x1.40mm_HandSolder, F.Cu at (277.9, 224.8)
- added R78: 15K, Resistor_SMD:R_0805_2012Metric_Pad1.20x1.40mm_HandSolder, F.Cu at (285.9, 213.7)
- added R79: 15K, Resistor_SMD:R_0805_2012Metric_Pad1.20x1.40mm_HandSolder, F.Cu at (292.6, 209.6)
- added R8: 16,9K, Resistor_SMD:R_0805_2012Metric_Pad1.20x1.40mm_HandSolder, F.Cu at (246.9, 199.8)
- added R80: 100, Resistor_SMD:R_0805_2012Metric_Pad1.20x1.40mm_HandSolder, F.Cu at (282.7, 224.8)
- added R81: 100, Resistor_SMD:R_0805_2012Metric_Pad1.20x1.40mm_HandSolder, F.Cu at (290.7, 213.7)
- added R82: 100, Resistor_SMD:R_0805_2012Metric_Pad1.20x1.40mm_HandSolder, F.Cu at (280.8, 227.7)
- added R83: 100, Resistor_SMD:R_0805_2012Metric_Pad1.20x1.40mm_HandSolder, F.Cu at (297.3, 209.6)
- added R84: 100, Resistor_SMD:R_0805_2012Metric_Pad1.20x1.40mm_HandSolder, F.Cu at (287.4, 223.7)
- added R85: 100, Resistor_SMD:R_0805_2012Metric_Pad1.20x1.40mm_HandSolder, F.Cu at (295.4, 212.6)
- added R86: 10K, Resistor_SMD:R_0805_2012Metric_Pad1.20x1.40mm_HandSolder, F.Cu at (247.0, 236.2)
- added R87: 10K, Resistor_SMD:R_0805_2012Metric_Pad1.20x1.40mm_HandSolder, F.Cu at (247.0, 233.3)
- added R88: 10K, Resistor_SMD:R_0805_2012Metric_Pad1.20x1.40mm_HandSolder, F.Cu at (264.5, 212.6)
- added R89: 1,5K, Resistor_SMD:R_0805_2012Metric_Pad1.20x1.40mm_HandSolder, F.Cu at (257.4, 225.7)
- added R9: 10K, Resistor_SMD:R_0805_2012Metric_Pad1.20x1.40mm_HandSolder, F.Cu at (298.6, 247.0)
- added R90: 10K, Resistor_SMD:R_0805_2012Metric_Pad1.20x1.40mm_HandSolder, F.Cu at (259.7, 215.5)
- added R91: 50, Resistor_SMD:R_0805_2012Metric_Pad1.20x1.40mm_HandSolder, F.Cu at (251.5, 230.3)
- added R92: 50, Resistor_SMD:R_0805_2012Metric_Pad1.20x1.40mm_HandSolder, F.Cu at (234.5, 247.8)
- added R93: 50, Resistor_SMD:R_0805_2012Metric_Pad1.20x1.40mm_HandSolder, F.Cu at (259.7, 209.6)
- added R94: 50, Resistor_SMD:R_0805_2012Metric_Pad1.20x1.40mm_HandSolder, F.Cu at (229.7, 247.8)
- added R95: 270, Resistor_SMD:R_0805_2012Metric_Pad1.20x1.40mm_HandSolder, F.Cu at (264.5, 209.6)
- added R96: 270, Resistor_SMD:R_0805_2012Metric_Pad1.20x1.40mm_HandSolder, F.Cu at (225.9, 244.8)
- added R97: 10K, Resistor_SMD:R_0805_2012Metric_Pad1.20x1.40mm_HandSolder, F.Cu at (246.8, 230.3)
- added R98: 33, Resistor_SMD:R_0805_2012Metric_Pad1.20x1.40mm_HandSolder, F.Cu at (225.0, 248.0)
- added R99: 33, Resistor_SMD:R_0805_2012Metric_Pad1.20x1.40mm_HandSolder, F.Cu at (230.7, 244.8)
- added RL1: G2RL-1-E-DC5, Relay_THT:Relay_DPDT_Omron_G2RL, F.Cu at (314.7, 110.0)
- added S1: KS-01Q-01_Obsolete, digikey-footprints:PushButton_Round_D12mm_THT_KS-01Q-01, F.Cu at (1.79, 43.1)
- added SW1: SW_PUSHBUTTON, digikey-footprints:PinHeader_1x2_P2.54mm, F.Cu at (266.2, 175.1)
- added SW2: SW_PUSHBUTTON, digikey-footprints:PinHeader_1x2_P2.54mm, F.Cu at (276.6, 175.1)
- added SW3: SW_PUSHBUTTON, digikey-footprints:PinHeader_1x2_P2.54mm, F.Cu at (287.1, 175.2)
- added SW4: SW_PUSHBUTTON, digikey-footprints:PinHeader_1x2_P2.54mm, F.Cu at (296.5, 175.2)
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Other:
- board size 294.6 x 143.3 mm -> 291.6 x 143.3 mm

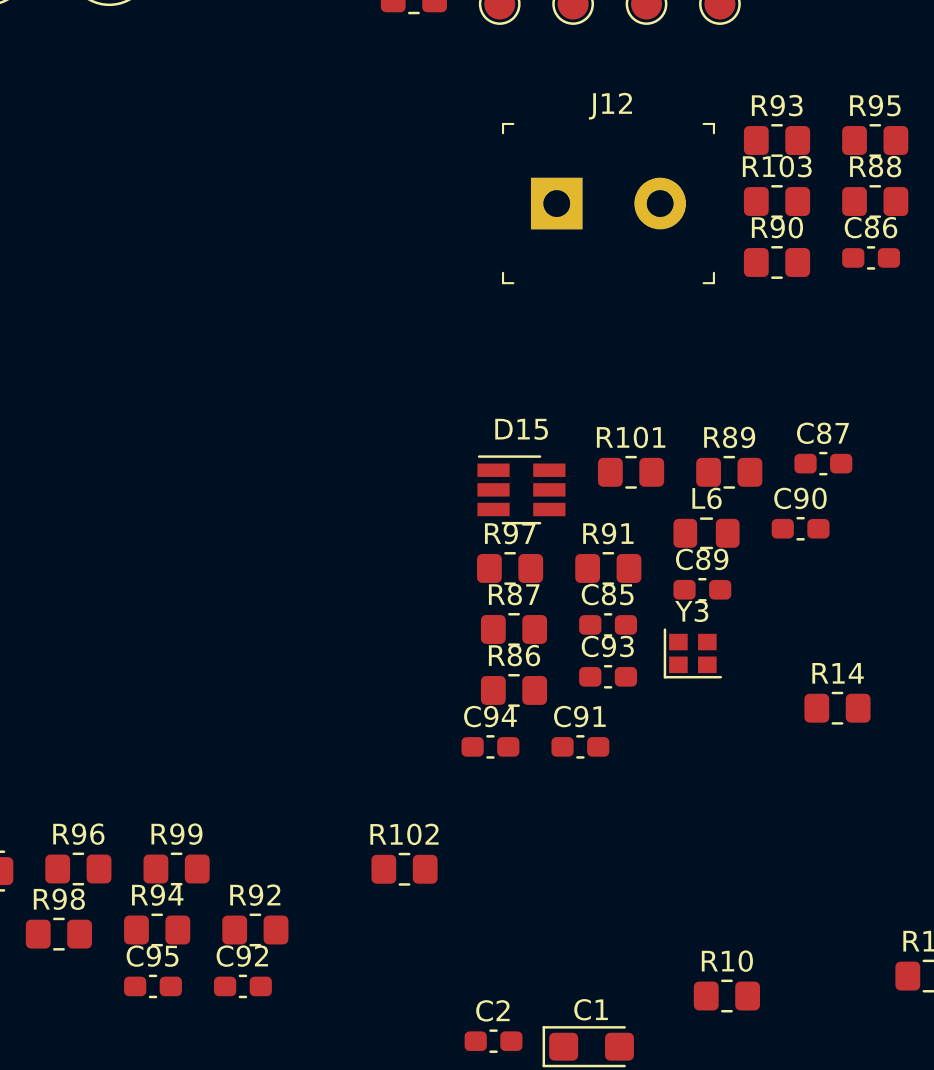
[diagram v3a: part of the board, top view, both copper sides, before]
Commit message: corrected few footprints, correct all resistors and capacitors type for ordering
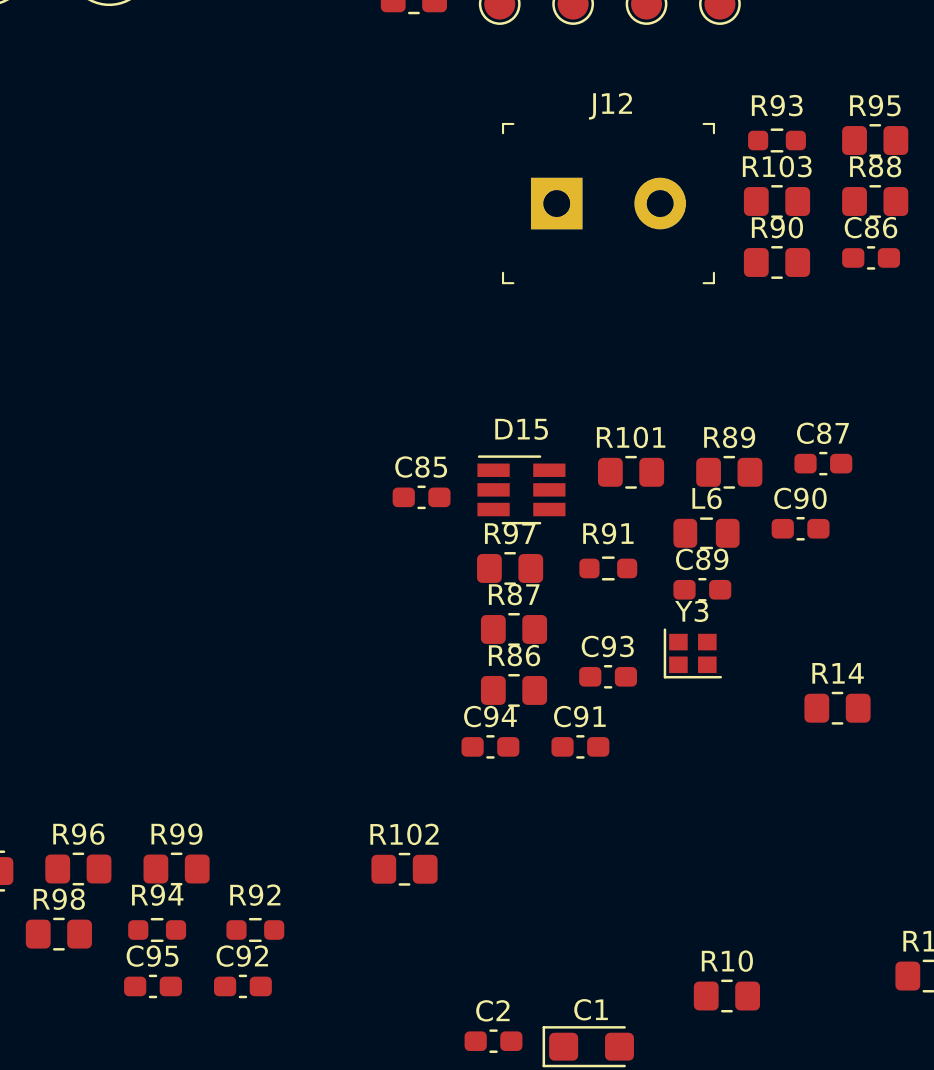
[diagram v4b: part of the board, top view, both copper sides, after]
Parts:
- R91, R92, R93, R94: footprint Resistor_SMD:R_0805_2012Metric_Pad1.20x1.40mm_HandSolder -> Resistor_SMD:R_0603_1608Metric_Pad0.98x0.95mm_HandSolder
- moved C85 10.9 mm to (242.5, 226.9)

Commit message: corrected footprint for B82790C0225N265
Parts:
- D1, D2: moved to B.Cu
- L3, L4, L5: footprint Inductor_SMD:L_CommonMode_Delevan_4222 -> SVIELCOM:B82790C0225N265
- SW1: value SW_PUSHBUTTON -> "+"
- SW2: value SW_PUSHBUTTON -> "-"
- SW3: value SW_PUSHBUTTON -> "Em/n"
- SW4: value SW_PUSHBUTTON -> "Clock"
- SW5: value SW_PUSHBUTTON -> "p/H"
- SW6: value SW_PUSHBUTTON -> "Func"
- moved L5 335.6 mm to (261.1, 233.3)
- moved D9 335.3 mm to (218.8, 248.7)
- moved R44 331.5 mm to (218.6, 242.8)
- moved D10 331.1 mm to (204.3, 248.8)
- moved C60 313.4 mm to (212.3, 228.5)
- moved L4 312.4 mm to (223.3, 233.6)
- moved R65 306.0 mm to (268.0, 221.7)
- moved C63 304.5 mm to (233.2, 238.4)
- moved C64 291.8 mm to (211.1, 239.5)
- moved C59 285.2 mm to (213.1, 234.6)
- moved S1 282.5 mm to (281.7, 81.3)
- moved TP13 278.9 mm to (203.5, 243.6)
- moved U21 277.6 mm to (223.4, 219.7), turned to 90 degrees
- moved U27 273.3 mm to (261.1, 220.1), turned to 90 degrees
- moved C62 271.3 mm to (217.7, 216.8), turned to 90 degrees
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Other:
- outline, holes or cut-outs redrawn

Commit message: PCB layout continue with SD_CARD interface TXS0206
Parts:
- moved J7 282.3 mm to (373.1, 98.0)
- moved R64 261.0 mm to (365.4, 221.2)
- moved PS3 259.2 mm to (325.5, 209.0)
- moved R27 257.6 mm to (375.3, 149.5)
- moved Q3 250.4 mm to (363.3, 69.5)
- moved D4 249.3 mm to (391.8, 127.4)
- moved C54 246.1 mm to (374.9, 136.5)
- moved LS1 242.2 mm to (330.6, 36.4)
- moved D5 241.8 mm to (375.2, 143.3)
- moved R63 222.7 mm to (331.1, 230.0)
- moved R23 219.7 mm to (375.7, 155.4)
- moved D8 216.9 mm to (377.6, 57.7)
- moved Q4 216.4 mm to (317.1, 34.8)
- moved PS2 212.0 mm to (206.2, 259.2)
- moved R26 207.3 mm to (383.5, 136.8)
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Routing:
- net (no net): vias 0 -> 1
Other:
- rule via_min_size: 0.3 -> 0.6

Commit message: Prepare to move analog decoupling to standalone PCB
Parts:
- added R104: 10K, Resistor_SMD:R_0805_2012Metric_Pad1.20x1.40mm_HandSolder, F.Cu at (121.0, 190.7)
- added R105: 10K, Resistor_SMD:R_0805_2012Metric_Pad1.20x1.40mm_HandSolder, F.Cu at (121.0, 193.7)
- added R106: 10K, Resistor_SMD:R_0805_2012Metric_Pad1.20x1.40mm_HandSolder, F.Cu at (125.8, 190.7)
- added R107: 50K, Resistor_SMD:R_0805_2012Metric_Pad1.20x1.40mm_HandSolder, F.Cu at (121.0, 196.6)
- added R108: 50K, Resistor_SMD:R_0805_2012Metric_Pad1.20x1.40mm_HandSolder, F.Cu at (125.8, 193.7)
- added R109: 50K, Resistor_SMD:R_0805_2012Metric_Pad1.20x1.40mm_HandSolder, F.Cu at (130.5, 190.7)
- added R110: 50K, Resistor_SMD:R_0805_2012Metric_Pad1.20x1.40mm_HandSolder, F.Cu at (121.0, 199.6)
- added R111: 10K, Resistor_SMD:R_0805_2012Metric_Pad1.20x1.40mm_HandSolder, F.Cu at (125.8, 196.6)
- C10, C7: value 2,7pF -> 2.7pF
- C14, C54, C55, C63, C66, C74, C76, C79, C80, C81, C82, C83, C84: value 0,1µF -> 0.1µF
- C29, C30: value 2,2µF -> 2.2µF
- C5, C6: value 4,6pF -> 4.6pF
- C56, C64, C77: value 0,22µF -> 0.22µF
- C92, C95: value 5,6pF -> 5.6pF
- L1, L2, L6: value 600R@100MHz [BK2125HS601-T] -> 600R@100MHz
- R103: value 12,1K -> 12.1K
- R14, R15: value 5,1K -> 5.1K
- R24, R35, R41, R51, R58, R69: value 3,3K -> 3.3K; footprint Resistor_SMD:R_0805_2012Metric_Pad1.20x1.40mm_HandSolder -> Resistor_SMD:R_0603_1608Metric_Pad0.98x0.95mm_HandSolder
- R25, R32, R42, R48, R59, R66: footprint Resistor_SMD:R_0805_2012Metric_Pad1.20x1.40mm_HandSolder -> Resistor_SMD:R_0603_1608Metric_Pad0.98x0.95mm_HandSolder
- R30, R46, R64: value 1,1K -> 1.1K
- R6, R8: value 16,9K -> 16.9K
- R89: value 1,5K -> 1.5K
- SW1: value "+" -> SW_PUSHBUTTON
- SW2: value "-" -> SW_PUSHBUTTON
- SW3: value "Em/n" -> SW_PUSHBUTTON
- SW4: value "Clock" -> SW_PUSHBUTTON
- SW5: value "p/H" -> SW_PUSHBUTTON
- SW6: value "Func" -> SW_PUSHBUTTON
- U14: value TXS0206-29YFPRB -> SN74AVCA406DGGR; footprint SVIELCOM:TXS0206-29YFPRB -> SVIELCOM:SN74AVCA406DGGR
- moved C11 247.8 mm to (86.0, 118.1)
- moved U12 247.8 mm to (86.0, 109.8)
- moved U13 247.8 mm to (73.9, 109.9)
- moved J2 247.8 mm to (76.9, 95.2)
- moved C17 209.4 mm to (77.1, 124.8)
- moved JP2 204.8 mm to (72.8, 130.5)
- moved U9 201.9 mm to (81.4, 131.0)
- moved C16 196.1 mm to (72.2, 125.0)
- moved C15 178.3 mm to (73.2, 118.7)
- moved L2 172.6 mm to (113.0, 125.7)
- moved C30 171.9 mm to (124.7, 157.9)
- moved C12 170.9 mm to (88.5, 124.3)
- moved C37 163.7 mm to (115.8, 142.7)
- moved C29 162.5 mm to (124.7, 154.7)
- moved C33 160.5 mm to (117.4, 131.9)
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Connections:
- C47 pad 1: +2,9V -> GNDREF
- J4 pad SWB: Net-(J4-PadSWB) -> /Microcontroller/SD_CARD_INS
- U11 pad 117: Net-(U11-Pad117) -> /Microcontroller/SD_CARD_CS
- U11 pad 118: Net-(U11-Pad118) -> /Microcontroller/SD_CARD_INS
- U11 pad 134: Net-(U11-Pad134) -> /Analog_and_digital_IO/ENCODER_A
- U11 pad 135: Net-(U11-Pad135) -> /Analog_and_digital_IO/ENCODER_B
- U11 pad 140: Net-(U11-Pad140) -> /Microcontroller/SDMMC1_CDIR
- U11 pad 96: /Analog_and_digital_IO/ENCODER_A -> /Microcontroller/SDMMC1_D0DIR
- U11 pad 97: /Analog_and_digital_IO/ENCODER_B -> /Microcontroller/SDMMC1_D123DIR
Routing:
- net GNDREF: track 0.40 -> 0.00 mm, vias 0 -> 8
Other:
- outline, holes or cut-outs redrawn
- net class Power: trace_width 0.6 -> 0.4
